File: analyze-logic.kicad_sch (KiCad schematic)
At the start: 27 parts

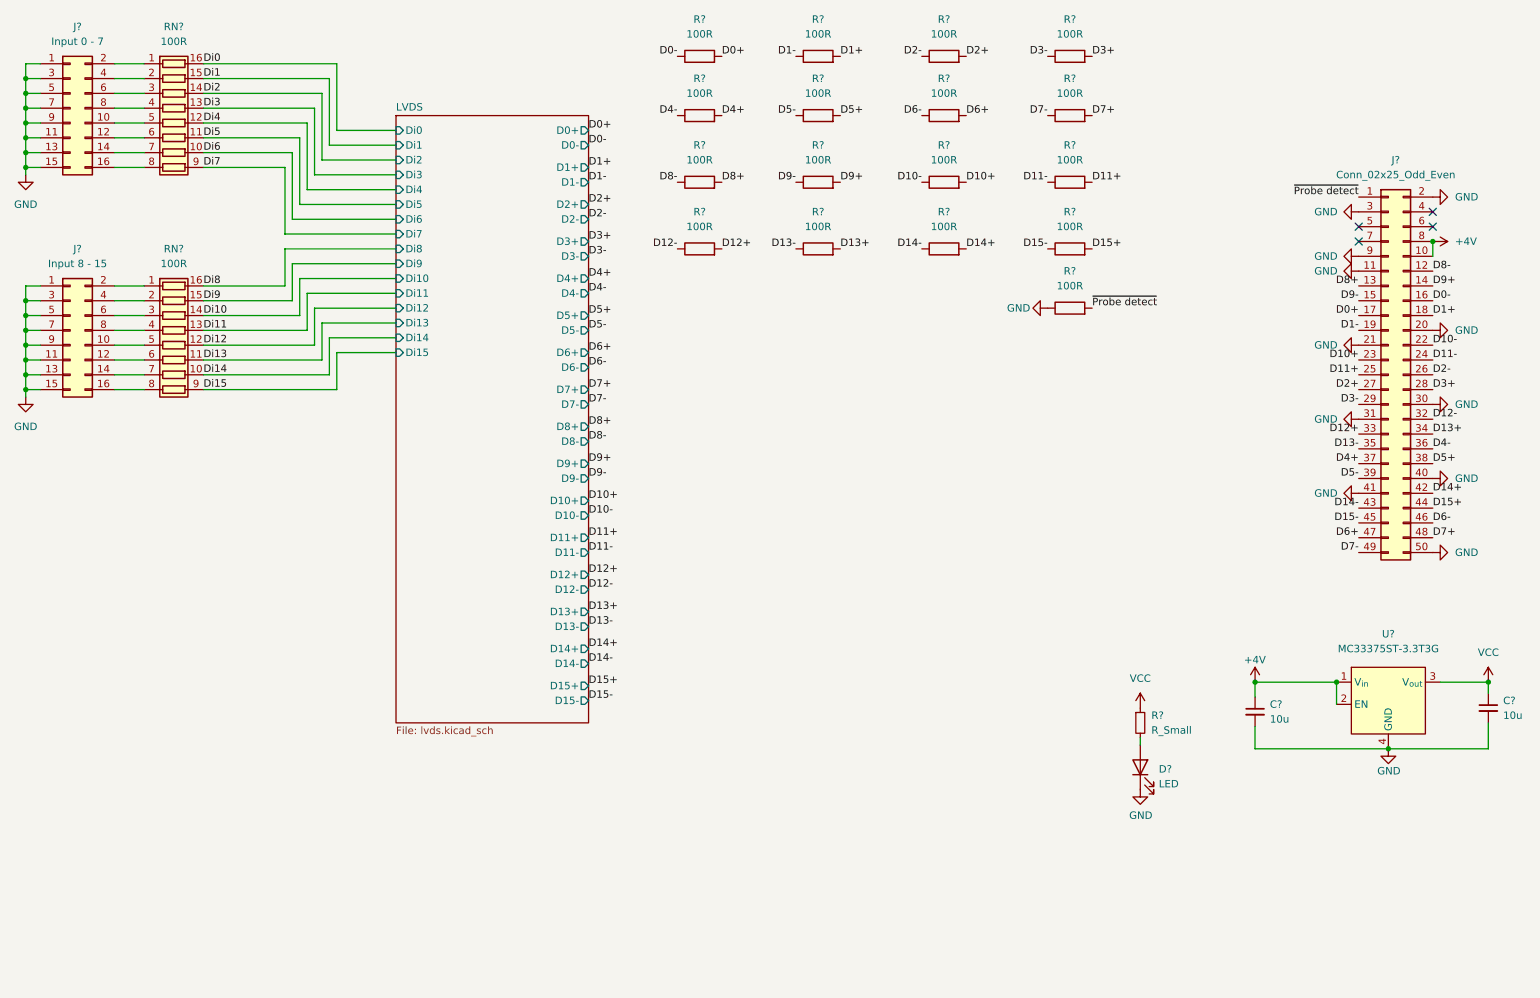
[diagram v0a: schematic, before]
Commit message: updated schematics
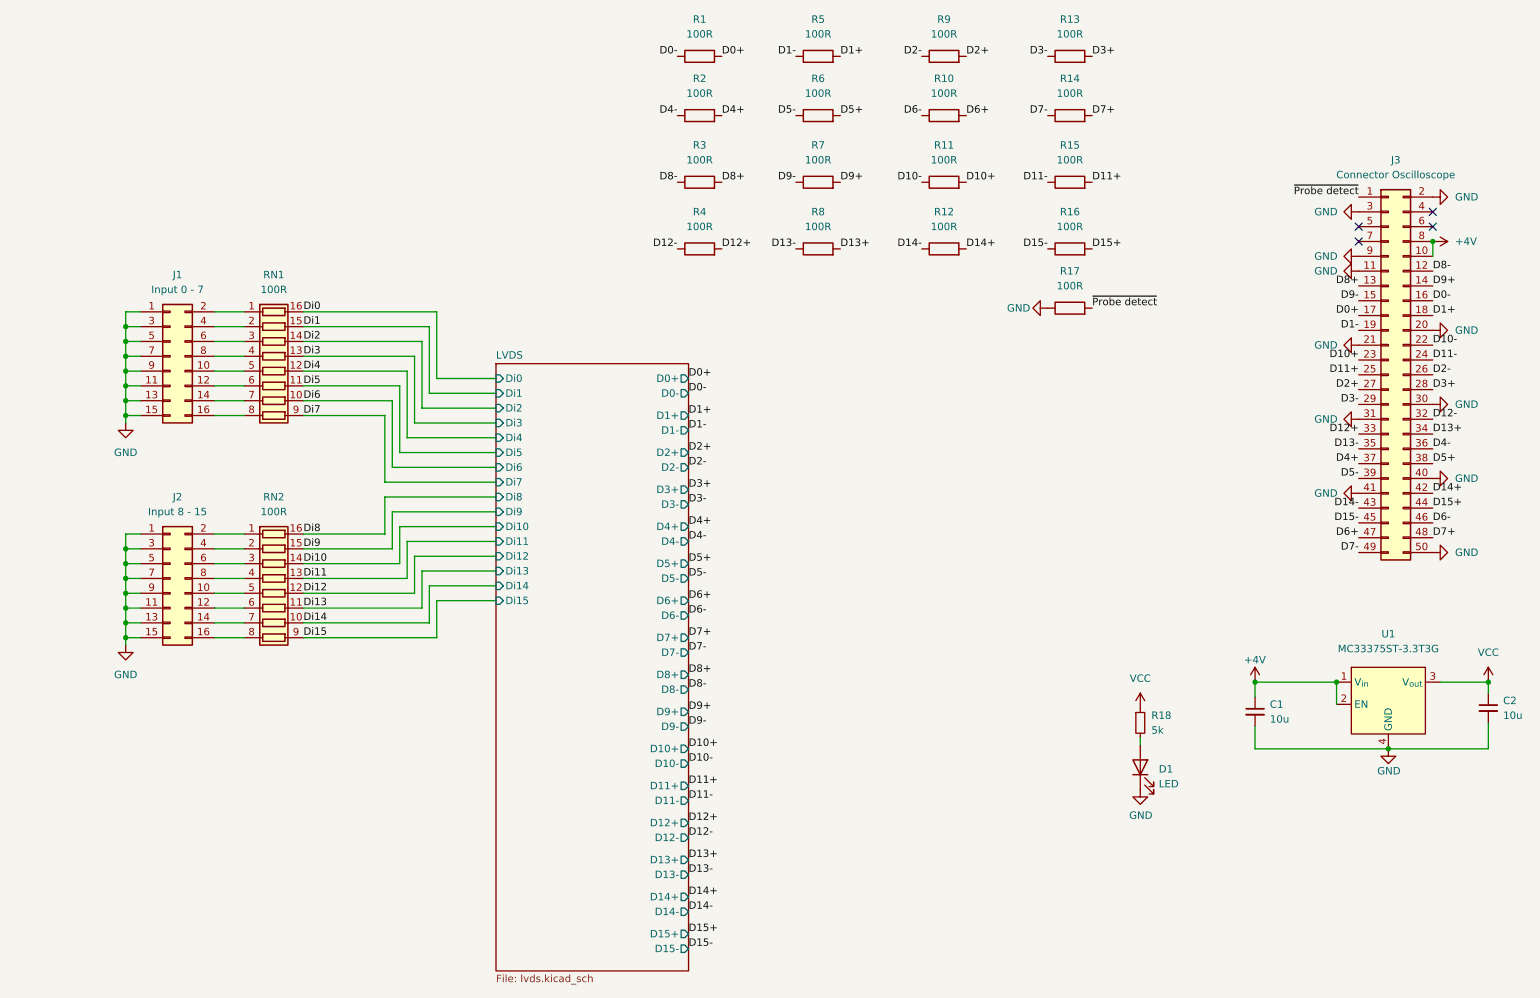
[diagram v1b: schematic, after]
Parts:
- D1: renamed from D?; MOUSER_NR (none) -> DNO
- J3: renamed from J?; value Conn_02x25_Odd_Even -> Connector Oscilloscope
- R18: renamed from R?; value R_Small -> 5k
- RN1, RN2: renamed from RN?; MOUSER_NR (none) -> 667-EXB-2HV101JV
- U1: renamed from U?; MOUSER_NR (none) -> 863-MC33375ST-3.3T3G
- gave numbers to parts that had none: 21
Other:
- moved on the sheet: J1, J2, RN1, RN2
